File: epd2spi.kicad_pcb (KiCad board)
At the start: 2 copper layers, 46 x 27 mm, 24 parts, among them J1 EPD_FPC, J2 Conn_01x08, Q1 SI1308EDL

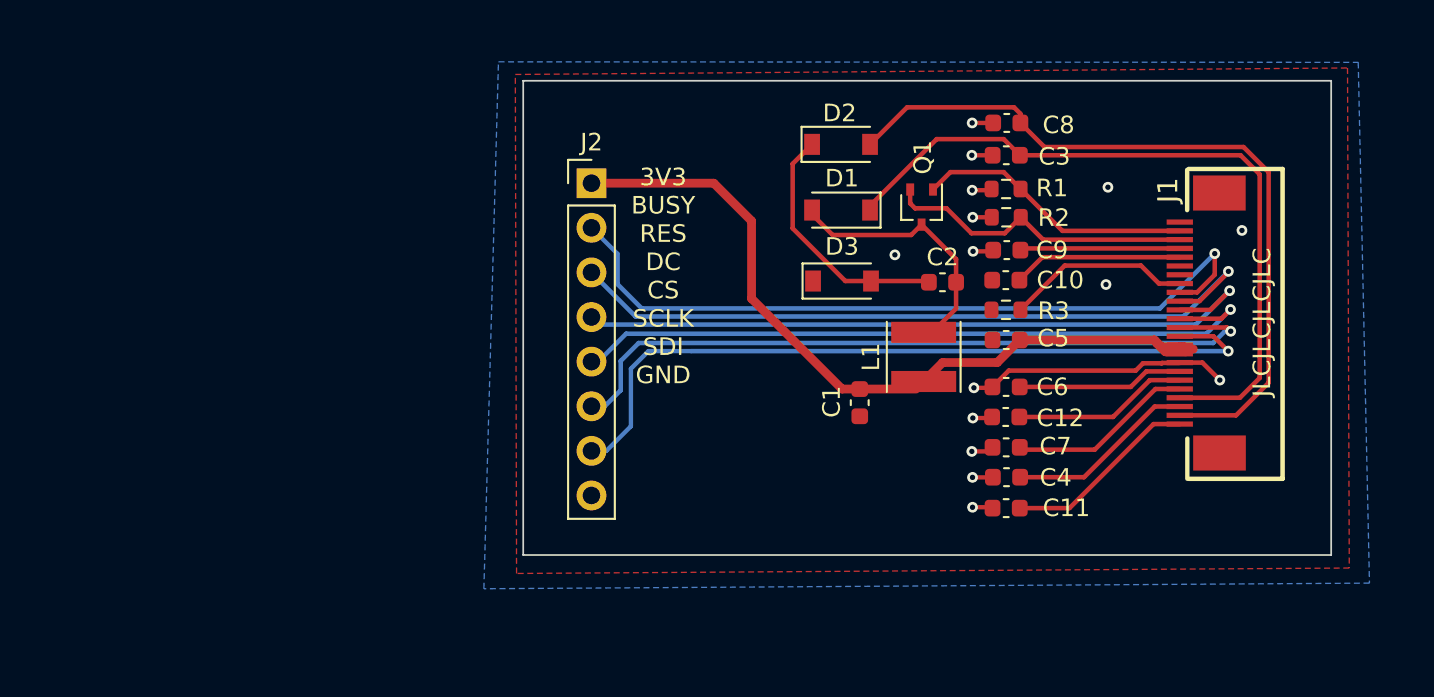
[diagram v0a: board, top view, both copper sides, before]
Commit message: Change the size and re-route
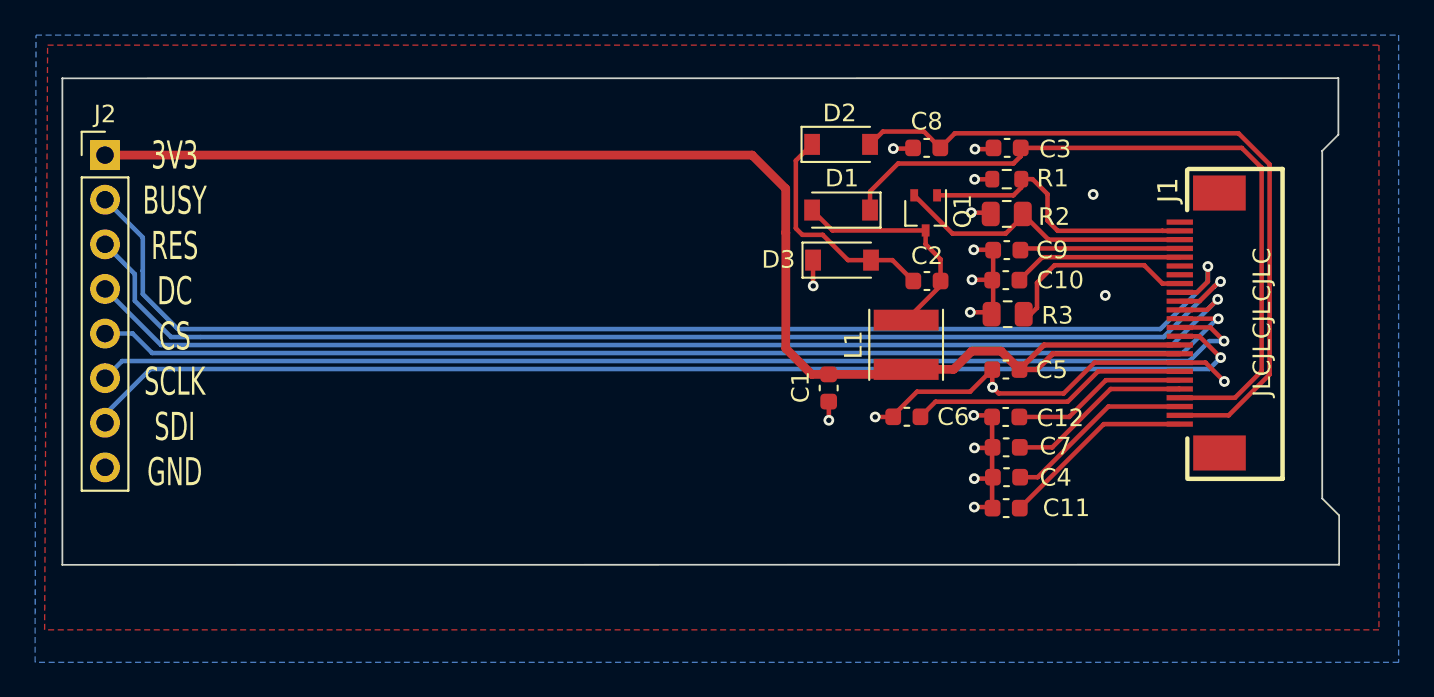
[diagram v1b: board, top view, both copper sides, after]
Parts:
- R2, R3: footprint Resistor_SMD:R_0603_1608Metric -> Resistor_SMD:R_0805_2012Metric
- moved J2 27.7 mm to (103.2, 83.2)
- moved C6 5.90 mm to (148.8, 98.1)
- moved C8 4.78 mm to (150.0, 82.8)
- moved C1 1.96 mm to (144.4, 96.5)
- moved C5 1.68 mm to (154.5, 95.4)
- moved L1 1.21 mm to (148.8, 94.0)
- moved D3 1.19 mm to (145.2, 89.2)
- moved C2 0.89 mm to (150.0, 90.4)
- moved G*** 0.78 mm to (139.1, 100.3)
- moved R1 0.56 mm to (154.5, 84.6)
- moved C3 0.42 mm to (154.6, 82.8)
- moved Q1 0.40 mm to (149.9, 86.5)
- moved R3 0.27 mm to (154.6, 92.3)
- moved R2 0.19 mm to (154.5, 86.6)
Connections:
- J1 pad 25: (no net) -> GND
- J1 pad 26: (no net) -> GND
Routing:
- net +3V3: track 46.7 -> 82.3 mm
- net EPD_BUSY: track 43.3 -> 72.4 mm
- net EPD_RES: track 41.9 -> 70.7 mm
- net EPD_DC: track 40.1 -> 68.2 mm
- net EPD_CS: track 40.3 -> 66.8 mm
- net EPD_SCLK: track 42.1 -> 67.4 mm
- net EPD_SDI: track 43.6 -> 67.7 mm
- net GND: track 24.7 -> 45.9 mm, vias 15 -> 18
- net Net-(C6-Pad1): track 9.48 -> 15.8 mm
- net Net-(C2-Pad2): track 14.5 -> 12.9 mm
- net Net-(C2-Pad1): track 14.2 -> 13.1 mm
- net /EPD_PREVGH: track 41.2 -> 42.0 mm
- net Net-(J1-Pad8): track 10.5 -> 11.3 mm
- net /EPD_GDR: track 15.8 -> 16.6 mm
- net /EPD_RESE: track 17.7 -> 17.0 mm
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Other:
- board size 46 x 27 mm -> 72.7 x 27.7 mm
